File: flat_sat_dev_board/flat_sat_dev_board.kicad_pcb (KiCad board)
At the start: 2 copper layers, 9.8 x 1.6 mm, 371 parts, among them IC1 RP2040_QFN56, IC2 PCT2075DP,118, IC3 PCT2075DP,118, IC4 LT3652IMSE#PBF, IC5 RP2040_QFN56, IC6 PCA9685PW,118, J1 RJ45_LED_Shielded, J10 Breakout, J11 Conn_Coaxial, J12 Foot0, J13 Bypass, J14 ISS Foot, J15 Foot1, J16 Heater, J17 Foot2, J18 Barrel_Jack_Switch, J19 BURN, J2 Life Makes Lemonade, J20 Foot3, J21 CHARGE, J22 RBF, J24 BM04B-SRSS-TB(LF)(SN), J25 Life Makes Lemonade, J26 Jetson, J27 BM04B-SRSS-TB(LF)(SN), J28 BM04B-SRSS-TB(LF)(SN), J29 CHARGE, J3 Conn_ARM_JTAG_SWD_10, J30 CAN1, J31 I2C Multiplexer Breakout, J32 I2C0 Breakout, J33 CAN2, J34 Screw_Terminal_01x02, J35 Conn_ARM_JTAG_SWD_10, J36 USB_B_Micro, J4 104031-0811, J5 BM04B-SRSS-TB(LF)(SN), J6 USB_B_Micro, J7 BM04B-SRSS-TB(LF)(SN), J8 Breakout, J9 FC to EPS Connector, K1 APAN3109, Q1 BSS138, Q10 NDS8434, Q11 MBT2222ADW1T1, Q12 MBT2222ADW1T1, Q2 MMBT2222AT, Q3 IRLML2803, Q4 IRLML2803, Q5 NDS8434, Q6 NDS8434, Q7 IRF7458, Q8 IRF7458, Q9 IRLML2803, SW1 KMR2, SW2 KMR2, SW3 KMR2, SW4 KMR2, U1 W25Q128JV, U10 RFM9xBreakout, U11 VL6180XV0NR/1, U12 LP5907-2.8V, U13 1049, U14 R5460N208AA, U15 1049, U16 TPS54226PWPRPWP14_2P31X2P46-L, U17 AD8495, U18 TLVH431 DBZ SOT-23, U19 INA219AxD, U2 MAX706RESA, U20 INA219AxD, U21 MAX706RESA, U22 ADS1015IDGS, U23 W25Q128JV, U24 MCP25625-E/ML, U25 TPS54226PWPRPWP14_2P31X2P46-L, U26 VEML7700, U27 DRV2605LDGS, U28 MCP9808_DFN, U29 VEML7700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

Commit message: layout on flat-sat board nearly done
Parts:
- removed C38: 10uf, Capacitor_SMD:C_0603_1608Metric
- removed C40: 1uf, Capacitor_SMD:C_0603_1608Metric
- removed R23: 10k, Resistor_SMD:R_0603_1608Metric
- removed TP5: 5V, TestPoint:TestPoint_Loop_D1.80mm_Drill1.0mm_Beaded
- removed U8: AP3602AKTR-G1, Package_TO_SOT_SMD:SOT-23-6
- added J37: Driver1, flat-sat:MOLEX_504050-0291, F.Cu at (119.1, 37.3)
- added J38: Driver2, flat-sat:MOLEX_504050-0291, F.Cu at (103.5, 37.4)
- added J39: Driver3, flat-sat:MOLEX_504050-0291, F.Cu at (80.1, 52.1)
- added J40: Driver4, flat-sat:MOLEX_504050-0291, F.Cu at (79.8, 69.0)
- C33, C35, J11, J3, J35, JP11, JP7, L1, U10, U11, U13, U15, U39, U9: moved to B.Cu
- J30: footprint Connector_JST:JST_SH_SM04B-SRSS-TB_1x04-1MP_P1.00mm_Horizontal -> Connector_JST:JST_SH_BM04B-SRSS-TB_1x04-1MP_P1.00mm_Vertical
- J33: value CAN2 -> Driver0; footprint Connector_JST:JST_SH_SM04B-SRSS-TB_1x04-1MP_P1.00mm_Horizontal -> flat-sat:MOLEX_504050-0291
- R40: value 629k -> 634k
- R43: value 415k -> 412k
- TP13: value TestPoint -> USBBOOT
- moved J1 182.8 mm to (195.4, 46.7), turned to 90 degrees
- moved C6 179.0 mm to (191.1, 36.6), turned to 180 degrees
- moved C44 176.7 mm to (209.8, 57.4), turned to 180 degrees
- moved C45 176.2 mm to (206.4, 56.8)
- moved C4 172.8 mm to (190.4, 41.7), turned to 180 degrees
- moved C3 172.4 mm to (190.9, 40.7), turned to 180 degrees
- moved R10 170.9 mm to (190.6, 47.2)
- moved C42 170.5 mm to (199.6, 54.5), turned to -90 degrees
- moved R6 170.4 mm to (190.6, 37.9)
- moved R8 170.3 mm to (190.6, 43.0)
- moved R9 170.2 mm to (190.6, 45.7)
- moved R28 168.4 mm to (212.3, 56.7), turned to -90 degrees
- moved R27 168.1 mm to (213.9, 56.7), turned to -90 degrees
- moved C12 167.8 mm to (191.2, 44.4), turned to 180 degrees
- moved R4 165.8 mm to (190.6, 39.4)
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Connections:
- J12 pad 1: Net-(J12-Pin_1) -> VBatt
- J12 pad 2: VBatt -> Net-(J12-Pin_2)
- J15 pad 1: VBatt1 -> Net-(J12-Pin_2)
- J15 pad 2: Net-(J12-Pin_1) -> VBatt1
- J16 pad 1: GND -> Heater
- J16 pad 2: Heater -> GND
- J17 pad 1: Net-(J17-Pin_1) -> VBatt
- J17 pad 2: VBatt -> Net-(J17-Pin_2)
- J19 pad 1: GND -> BURN
- J19 pad 2: BURN -> GND
- J20 pad 1: VBatt1 -> Net-(J17-Pin_2)
- J20 pad 2: Net-(J17-Pin_1) -> VBatt1
- J22 pad 1: VBUSP -> VBatt1
- J22 pad 2: VBatt1 -> VBUSP
- J33 pad 1: +3V3 -> Net-(J33-Pin_1)
- J33 pad 2: /Electrical Power System Stuff/CANH -> Net-(J33-Pin_2)
- U27 pad 7: Net-(U27-OUT+) -> Net-(J33-Pin_1)
- U27 pad 9: Net-(U27-OUT+) -> Net-(J33-Pin_2)
- U30 pad 7: Net-(U30-OUT+) -> Net-(J37-Pin_1)
- U30 pad 9: Net-(U30-OUT+) -> Net-(J37-Pin_2)
- U35 pad 7: Net-(U35-OUT+) -> Net-(J38-Pin_1)
- U35 pad 9: Net-(U35-OUT+) -> Net-(J38-Pin_2)
- U37 pad 7: Net-(U37-OUT+) -> Net-(J39-Pin_1)
- U37 pad 9: Net-(U37-OUT+) -> Net-(J39-Pin_2)
- U41 pad 7: Net-(U41-OUT+) -> Net-(J40-Pin_1)
- U41 pad 9: Net-(U41-OUT+) -> Net-(J40-Pin_2)
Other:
- board size 9.8 x 1.6 mm -> 141.6 x 116.1 mm
- copper layers 2 -> 4

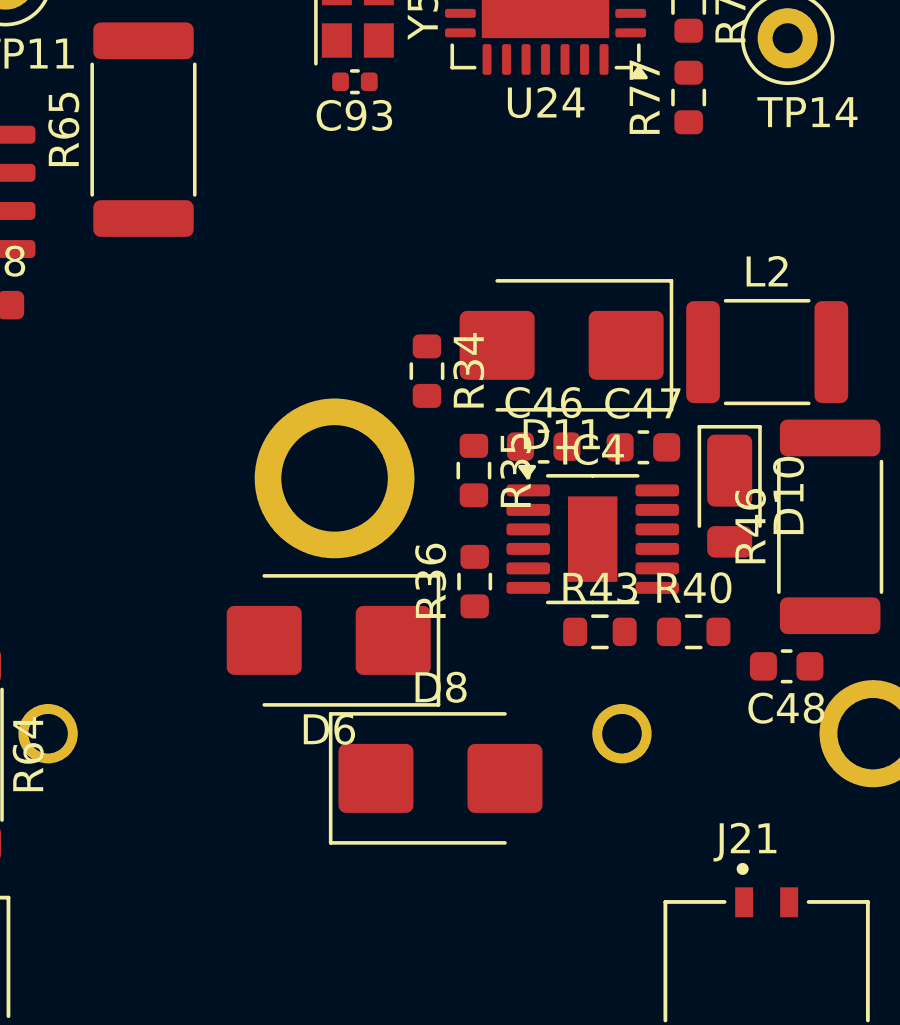
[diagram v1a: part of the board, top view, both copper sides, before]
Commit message: Updated Camera Board V2 with Production Files
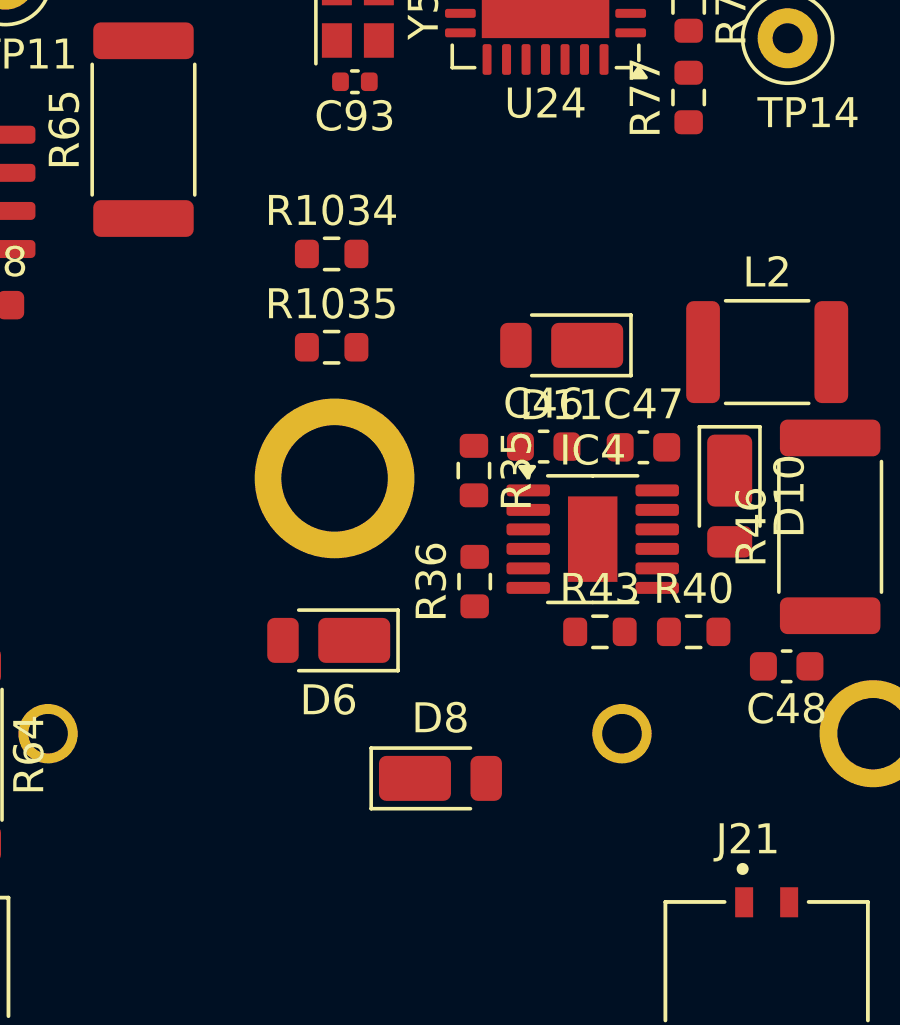
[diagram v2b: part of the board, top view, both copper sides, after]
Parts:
- removed R34: 200k, Resistor_SMD:R_0603_1608Metric
- added R1034: 100K, Resistor_SMD:R_0603_1608Metric, F.Cu at (156.0, 119.5)
- added R1035: 100K, Resistor_SMD:R_0603_1608Metric, F.Cu at (156.0, 122.6)
- D11, D6, D8: value D_Schottky -> DFLS130L; footprint Diode_SMD:D_SMB -> Diode_SMD:D_PowerDI-123
- J29: value CHARGE -> Solar Input
- J31: value I2C Multiplexer Breakout -> I2C0 Breakout
- J32: value I2C0 Breakout -> I2C1 Breakout
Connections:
- J17 pad 1: VBatt -> Net-(J17-Pin_1)
- J17 pad 2: Net-(J17-Pin_2) -> VBatt
- J20 pad 1: Net-(J17-Pin_2) -> VBatt1
- J20 pad 2: VBatt1 -> Net-(J17-Pin_1)

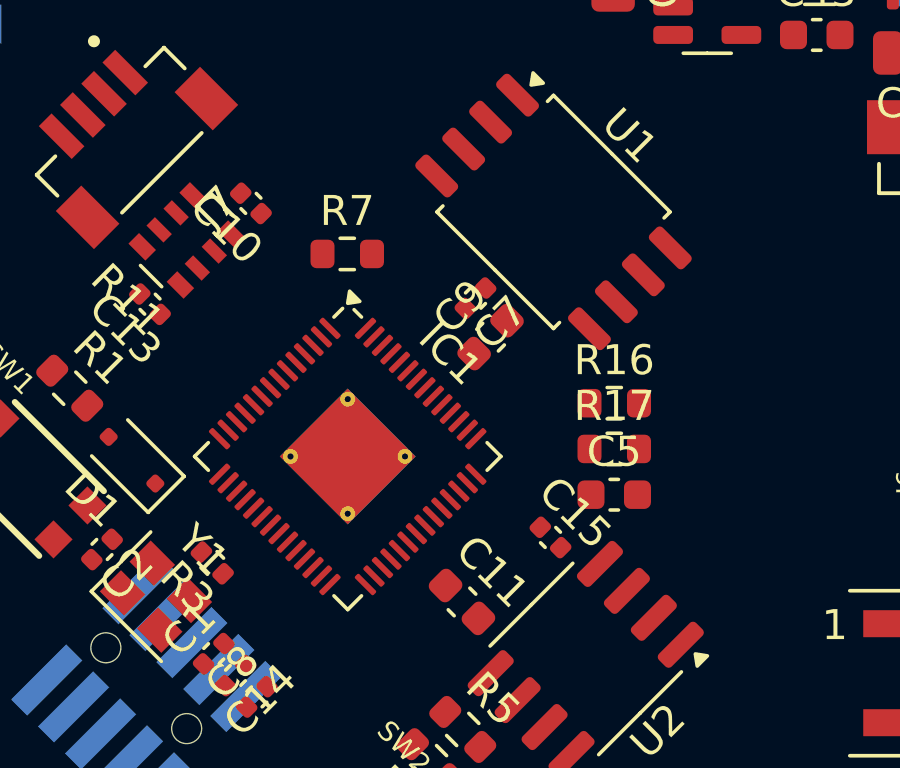
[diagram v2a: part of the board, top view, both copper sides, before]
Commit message: Fixed References From 3.3V to be all 3V3
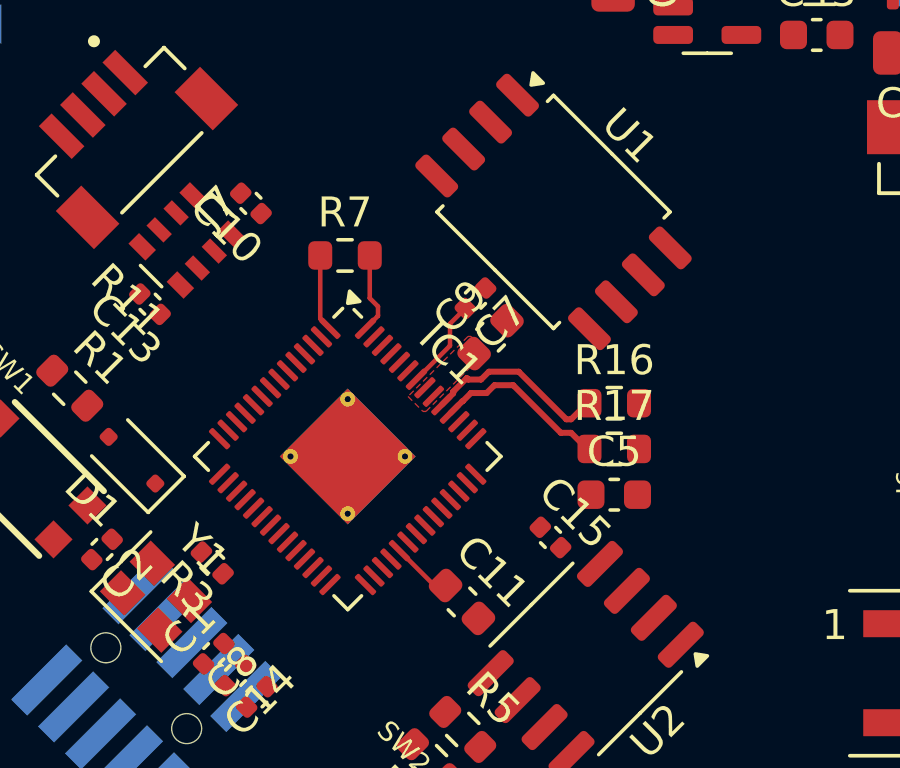
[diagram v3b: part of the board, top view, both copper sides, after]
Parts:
- moved R7 0.09 mm to (190.7, 64.1)
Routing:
- net /Flight Computer Stuff/D+: track 0.00 -> 6.33 mm
- net /Flight Computer Stuff/D-: track 0.00 -> 5.91 mm
- net +3V3: track 0.00 -> 4.58 mm
- net 1.2V: track 0.00 -> 3.04 mm
- net /Flight Computer Stuff/QSPI_CS: track 0.00 -> 2.72 mm
- added copper zone on F.Cu, net +3V3
